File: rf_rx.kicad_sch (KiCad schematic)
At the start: 12 parts, among them SW2 SW_Push_45deg

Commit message: refactor labels U and assigned resistance footprint
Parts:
- removed SW2: SW_Push_45deg, symbol Switch:SW_Push_45deg
- added SW2: SW_Push_Open, symbol Switch:SW_Push_Open
- R40, R41: footprint (none) -> Resistor_SMD:R_0603_1608Metric
- U10: renamed from U11; value ~ -> ME6217C33M5G
- U11: renamed from U12; value ~ -> ELRS_RX
- U12: renamed from U13; value ~ -> wifi_rf
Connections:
- net GND: now also SW2.2 (B)
- new net: SW2.1 (A), U11. (IO2)
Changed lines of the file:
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@@
 	(wire
 		(pts
-			(xy 156.21 151.13) (xy 156.21 153.67)
-		)
-		(stroke
-			(width 0)
-			(type default)
-		)
-	)
-	(wire
-		(pts
-			(xy 148.59 151.13) (xy 156.21 151.13)
+			(xy 156.21 146.05) (xy 156.21 153.67)
 		)
 		(stroke
@@
 		(pts
 			(xy 234.95 127) (xy 236.22 127)
+		)
+		(stroke
+			(width 0)
+			(type default)
+		)
+	)
+	(wire
+		(pts
+			(xy 156.21 146.05) (xy 153.67 146.05)
 		)
 		(stroke
@@
 	)
 	(symbol
-		(lib_id "Switch:SW_Push_45deg")
-		(at 146.05 148.59 0)
+		(lib_id "Switch:SW_Push_Open")
+		(at 148.59 146.05 0)
 		(unit 1)
 		(exclude_from_sim no)
@@
 		(fields_autoplaced yes)
 		(property "Reference" "SW2"
-			(at 146.05 140.97 0)
-			(effects
-				(font
-					(size 1.27 1.27)
-				)
-			)
-		)
-		(property "Value" "SW_Push_45deg"
-			(at 146.05 143.51 0)
+			(at 148.59 139.7 0)
+			(effects
+				(font
+					(size 1.27 1.27)
+				)
+			)
+		)
+		(property "Value" "SW_Push_Open"
+			(at 148.59 142.24 0)
 			(effects
 				(font
@@
 		)
 		(property "Footprint" ""
-			(at 146.05 148.59 0)
+			(at 148.59 140.97 0)
 			(effects
 				(font
@@
 		)
 		(property "Datasheet" "~"
-			(at 146.05 148.59 0)
-			(effects
-				(font
-					(size 1.27 1.27)
-				)
-				(hide yes)
-			)
-		)
-		(property "Description" "Push button switch, normally open, two pins, 45° tilted"
-			(at 146.05 148.59 0)
-			(effects
-				(font
-					(size 1.27 1.27)
-				)
-				(hide yes)
-			)
+			(at 148.59 140.97 0)
+			(effects
+				(font
+					(size 1.27 1.27)
+				)
+				(hide yes)
+			)
+		)
+		(property "Description" "Push button switch, push-to-open, generic, two pins"
+			(at 148.59 146.05 0)
+			(effects
+				(font
+					(size 1.27 1.27)
+				)
+				(hide yes)
+			)
+		)
+		(pin "1"
 		)
 		(pin "2"
 		)
-		(pin "1"
-		)
 		(instances
-			(project "fch7"
+			(project ""
 				(path "/11716af6-0e6e-444b-b738-3f12da23c1a2/c005db94-b190-4389-8874-35307c577c05"
 					(reference "SW2")
@@
 		(on_board yes)
 		(dnp no)
-		(fields_autoplaced yes)
-		(property "Reference" "U13"
-			(at 221.615 92.71 0)
-			(effects
-				(font
-					(size 1.27 1.27)
-				)
-			)
-		)
-		(property "Value" "~"
-			(at 221.615 95.25 0)
+		(property "Reference" "U12"
+			(at 221.488 90.678 0)
+			(effects
+				(font
+					(size 1.27 1.27)
+				)
+			)
+		)
+		(property "Value" "wifi_rf"
+			(at 221.742 92.964 0)
 			(effects
 				(font
@@
 			(project "fch7"
 				(path "/11716af6-0e6e-444b-b738-3f12da23c1a2/c005db94-b190-4389-8874-35307c577c05"
-					(reference "U13")
+					(reference "U12")
 					(unit 1)
 				)
@@
 		(dnp no)
 		(fields_autoplaced yes)
-		(property "Reference" "U11"
+		(property "Reference" "U10"
 			(at 94.615 43.18 0)
 			(effects
@@
 			)
 		)
-		(property "Value" "~"
+		(property "Value" "ME6217C33M5G"
 			(at 94.615 45.72 0)
 			(effects
@@
 			(project "fch7"
 				(path "/11716af6-0e6e-444b-b738-3f12da23c1a2/c005db94-b190-4389-8874-35307c577c05"
-					(reference "U11")
+					(reference "U10")
 					(unit 1)
 				)
@@
 			)
 		)
-		(property "Footprint" ""
+		(property "Footprint" "Resistor_SMD:R_0603_1608Metric"
 			(at 60.452 134.62 90)
 			(effects
@@
 			)
 		)
-		(property "Footprint" ""
+		(property "Footprint" "Resistor_SMD:R_0603_1608Metric"
 			(at 164.592 74.93 90)
 			(effects
@@
 		(dnp no)
 		(fields_autoplaced yes)
-		(property "Reference" "U12"
+		(property "Reference" "U11"
 			(at 100.33 111.76 0)
 			(effects
@@
 			)
 		)
-		(property "Value" "~"
+		(property "Value" "ELRS_RX"
 			(at 100.33 114.3 0)
 			(effects
@@
 			(project "fch7"
 				(path "/11716af6-0e6e-444b-b738-3f12da23c1a2/c005db94-b190-4389-8874-35307c577c05"
-					(reference "U12")
+					(reference "U11")
 					(unit 1)
 				)

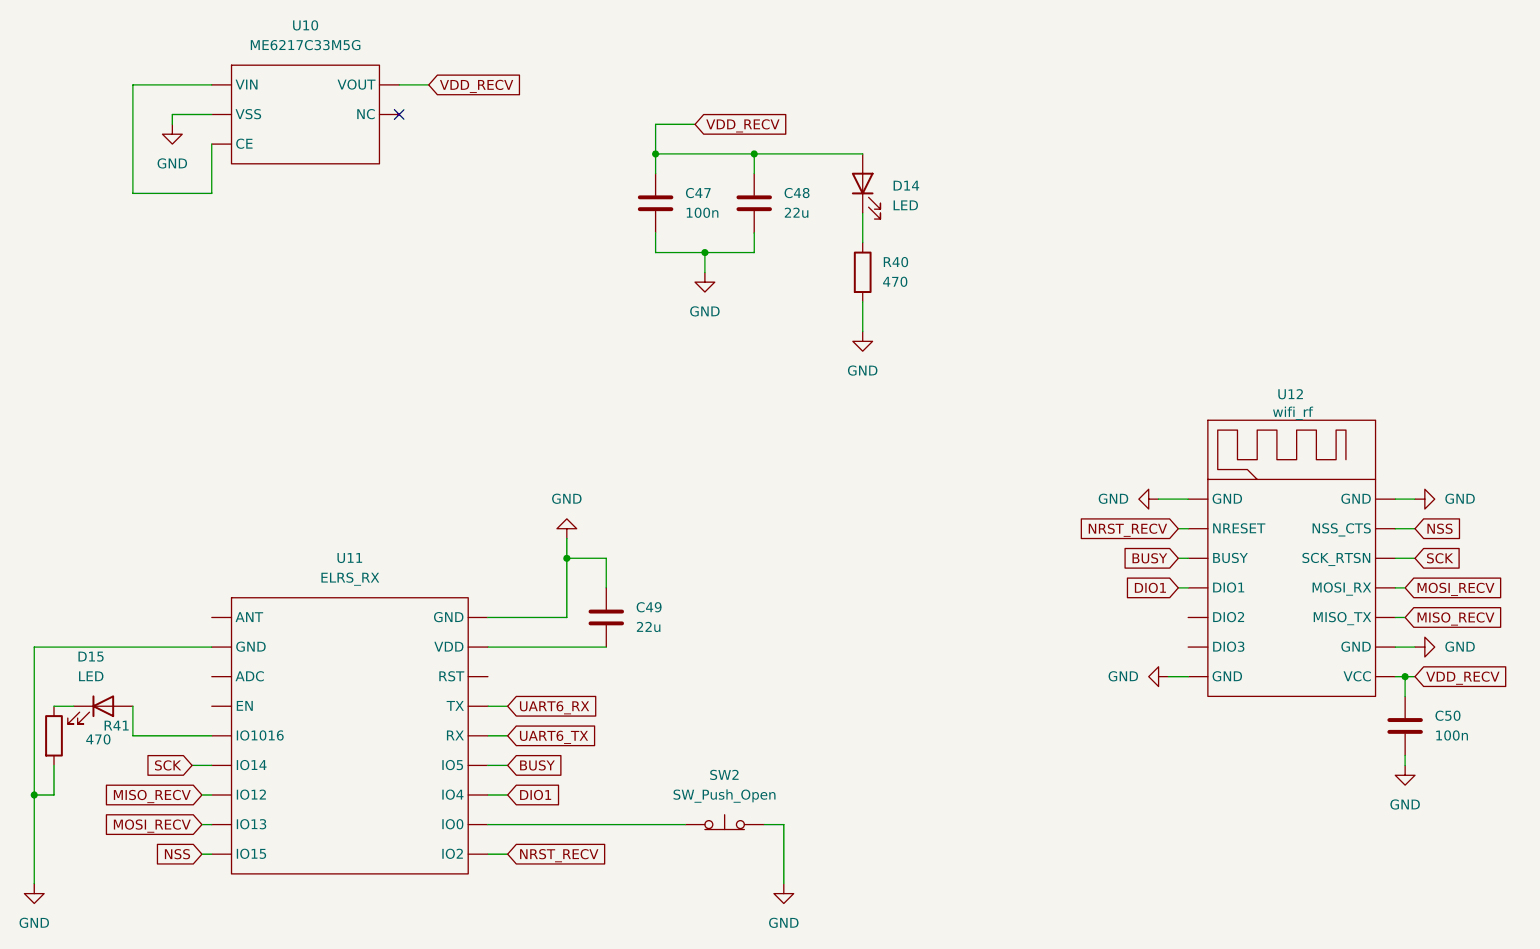
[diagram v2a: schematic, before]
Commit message: refactor and update references, added some footprints
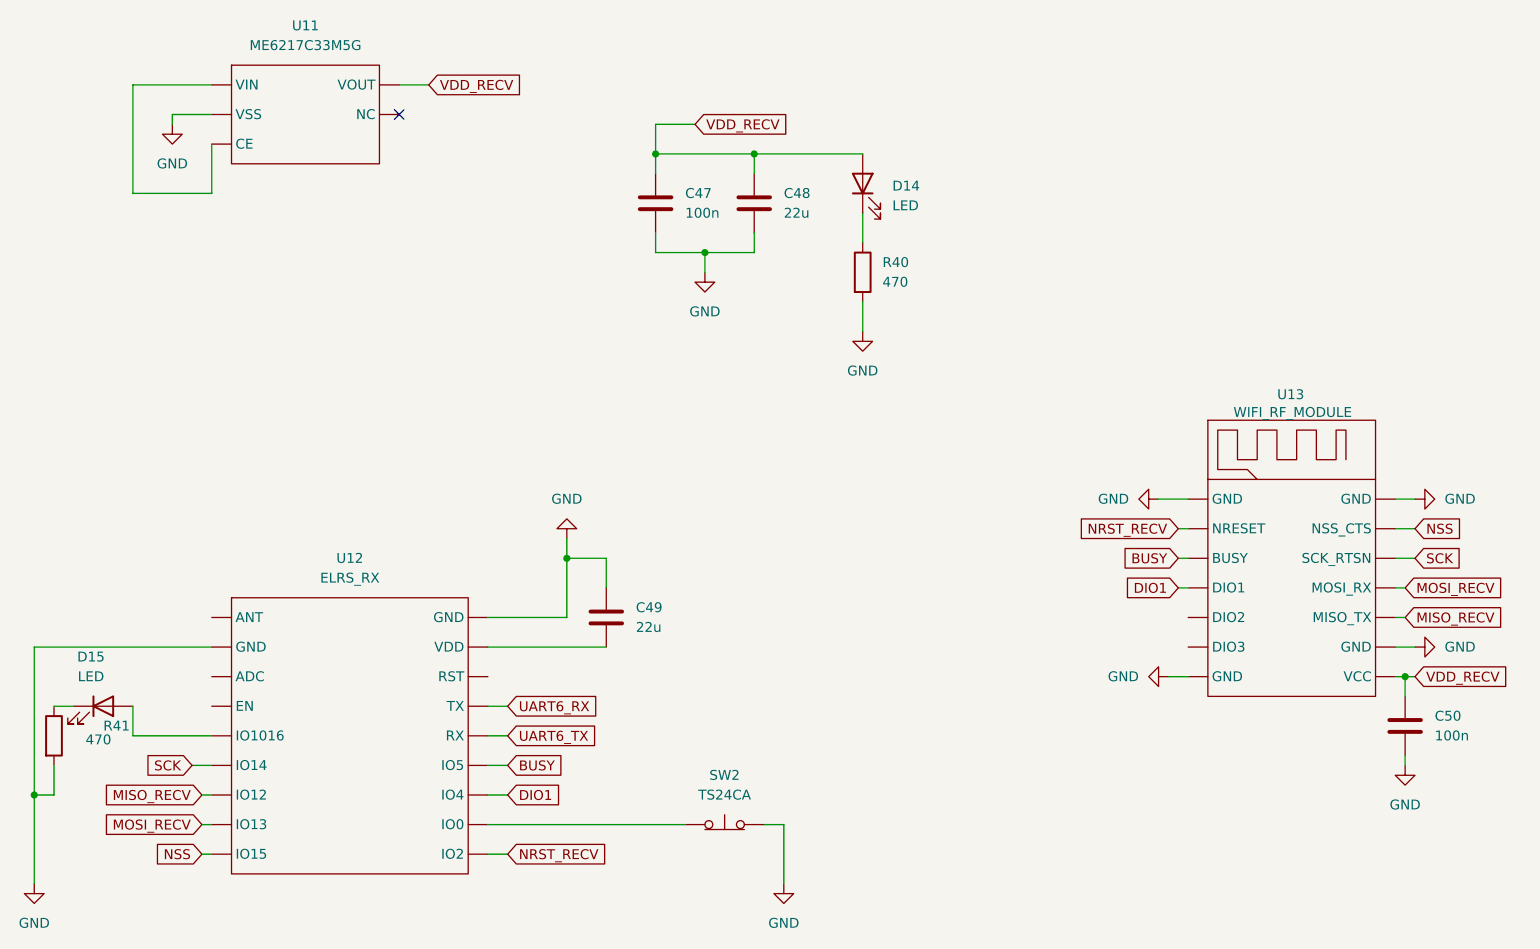
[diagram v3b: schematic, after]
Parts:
- C47, C50: footprint (none) -> Capacitor_SMD:C_0603_1608Metric
- C48, C49: footprint (none) -> Capacitor_SMD:C_1210_3225Metric
- D14, D15: footprint (none) -> Diode_SMD:D_SOD-323
- SW2: value SW_Push_Open -> TS24CA
- U13: renamed from U12; value wifi_rf -> WIFI_RF_MODULE
- renumbered U10 to U11, U11 to U12
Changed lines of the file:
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@@
 			)
 		)
-		(property "Footprint" ""
+		(property "Footprint" "Capacitor_SMD:C_1210_3225Metric"
 			(at 153.3652 69.85 0)
 			(effects
@@
 			)
 		)
-		(property "Footprint" ""
+		(property "Footprint" "Capacitor_SMD:C_0603_1608Metric"
 			(at 237.1852 137.16 0)
 			(effects
@@
 			)
 		)
-		(property "Footprint" ""
+		(property "Footprint" "Diode_SMD:D_SOD-323"
 			(at 68.58 130.81 0)
 			(effects
@@
 			)
 		)
-		(property "Value" "SW_Push_Open"
+		(property "Value" "TS24CA"
 			(at 148.59 142.24 0)
 			(effects
@@
 		(on_board yes)
 		(dnp no)
-		(property "Reference" "U12"
+		(property "Reference" "U13"
 			(at 221.488 90.678 0)
 			(effects
@@
 			)
 		)
-		(property "Value" "wifi_rf"
+		(property "Value" "WIFI_RF_MODULE"
 			(at 221.742 92.964 0)
 			(effects
@@
 			(project "fch7"
 				(path "/11716af6-0e6e-444b-b738-3f12da23c1a2/c005db94-b190-4389-8874-35307c577c05"
-					(reference "U12")
+					(reference "U13")
 					(unit 1)
 				)
@@
 		(dnp no)
 		(fields_autoplaced yes)
-		(property "Reference" "U10"
+		(property "Reference" "U11"
 			(at 94.615 43.18 0)
 			(effects
@@
 			(project "fch7"
 				(path "/11716af6-0e6e-444b-b738-3f12da23c1a2/c005db94-b190-4389-8874-35307c577c05"
-					(reference "U10")
+					(reference "U11")
 					(unit 1)
 				)
@@
 			)
 		)
-		(property "Footprint" ""
+		(property "Footprint" "Diode_SMD:D_SOD-323"
 			(at 166.37 63.5 0)
 			(effects
@@
 			)
 		)
-		(property "Footprint" ""
+		(property "Footprint" "Capacitor_SMD:C_1210_3225Metric"
 			(at 134.3152 123.19 0)
 			(effects
@@
 			)
 		)
-		(property "Footprint" ""
+		(property "Footprint" "Capacitor_SMD:C_0603_1608Metric"
 			(at 140.6652 69.85 0)
 			(effects
@@
 		(dnp no)
 		(fields_autoplaced yes)
-		(property "Reference" "U11"
+		(property "Reference" "U12"
 			(at 100.33 111.76 0)
 			(effects
@@
 			(project "fch7"
 				(path "/11716af6-0e6e-444b-b738-3f12da23c1a2/c005db94-b190-4389-8874-35307c577c05"
-					(reference "U11")
-					(unit 1)
-				)
+					(reference "U12")
+					(unit 1)
+				)
